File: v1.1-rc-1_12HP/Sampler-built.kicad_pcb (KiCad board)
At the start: 4 copper layers, 60.5 x 109.2 mm, 231 parts, among them J10 Eurorack_Power_10pin_Unshroud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, J11 3.5mm_Mono_Switched, J12 3.5mm_Mono_Switched, J13 3.5mm_Mono_Switched, J14 3.5mm_Mono_Switched, J15 3.5mm_Mono_Switched, J16 3.5mm_Mono_Switched, J17 3.5mm_Mono_Switched, J2 3.5mm_Mono_Switched, J3 Conn_01x04, J4 Conn_02x04, J6 3.5mm_Mono_Switched, J7 3.5mm_Mono_Switched, J8 3.5mm_Mono_Switched, J9 3.5mm_Mono_Switched, U1 TL072H, U10 TL072H, U11 TL072H, U12 TL072H, U13 AP62200WU-7, U14 TL072H, U15 TL072H, U16 TL072H, U2 STM32F746IE, U3 TL072H, U4 SDRAM_IS42S16400J-6BLI-TR, U5 TL072H, U6 NCP51460SN33, U8 TL072H, U9 PCM3060PW, Y1 16MHz_18pF_FA238

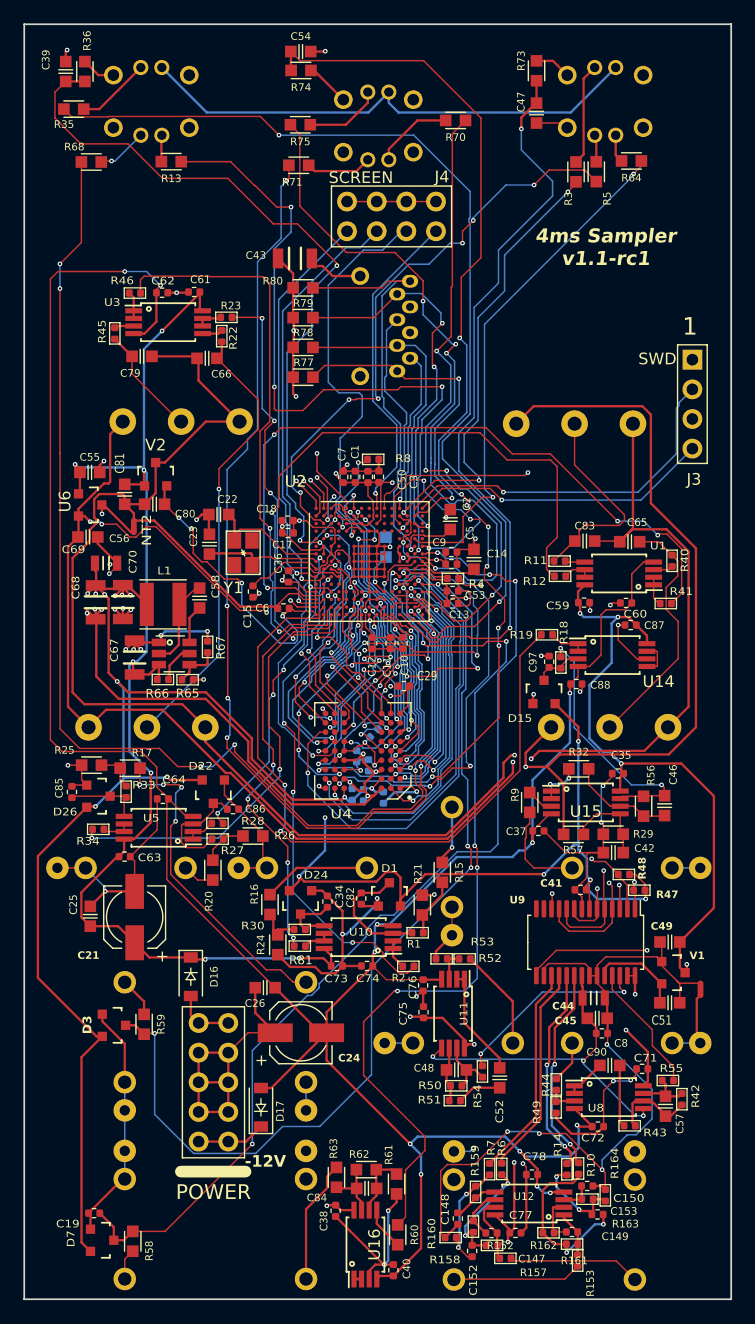
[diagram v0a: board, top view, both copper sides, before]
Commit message: v1.1rc-1 was accidentally updated from how it was produced. Reverted the folder back to an earlier commit
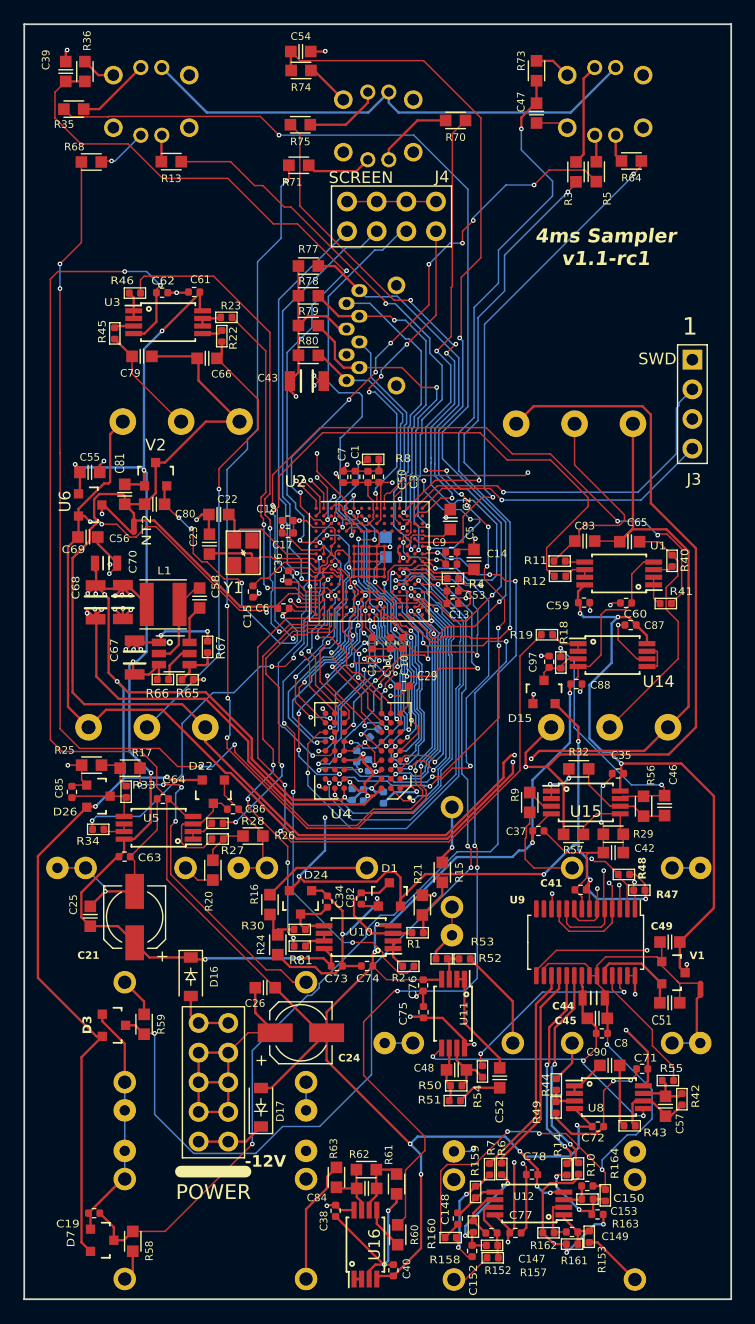
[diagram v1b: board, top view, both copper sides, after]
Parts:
- moved C43 10.6 mm to (159.9, 46.9)
- moved R77 9.53 mm to (160.0, 37.0)
- moved R80 5.80 mm to (160.0, 44.7)
- moved R78 4.44 mm to (160.0, 39.6)
- moved R153 2.27 mm to (184.0, 120.2)
- moved R152 1.09 mm to (175.8, 122.0), turned to 0 degrees
- moved R79 0.82 mm to (160.0, 42.1)
- turned SD1 to -90 degrees
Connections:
- R152 pad 1: Net-(J16-SIG) -> Net-(J17-SIG)
- R153 pad 1: Net-(J17-SIG) -> Net-(J16-SIG)
- R23 pad 2: /A7 -> /A3
- R28 pad 2: /A8 -> /A4
- R34 pad 2: /A4 -> /A8
- R41 pad 2: /A3 -> /A7
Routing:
- net /A3: track 63.8 -> 30.4 mm, vias 4 -> 2
- net /A7: track 31.2 -> 60.2 mm
- net /D17: track 35.2 -> 22.1 mm
- net /A4: track 37.1 -> 24.9 mm
- net /D3: track 58.6 -> 46.7 mm, vias 4 -> 2
- net /A8: track 25.7 -> 35.1 mm
- net /D19: track 14.8 -> 22.9 mm
- net Net-(J17-SIG): track 11.1 -> 3.61 mm
- net /D16: track 34.8 -> 28.5 mm, vias 3 -> 2
- net Net-(J16-SIG): track 11.4 -> 5.23 mm
- net /D18: track 28.9 -> 32.6 mm, vias 2 -> 1
- net /A9: track 48.1 -> 45.4 mm
- net /D1: track 50.1 -> 47.5 mm, vias 6 -> 8
- net GND: track 364.8 -> 362.5 mm, vias 57 -> 59
- net /A1: track 57.7 -> 59.8 mm
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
